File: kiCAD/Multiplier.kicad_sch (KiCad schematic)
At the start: 55 parts, among them IC2 ADG1221BRMZ, J1 Conn_01x02_Pin, J2 Conn_01x02_Pin, J3 Conn_01x01_Pin, Q1 BC846BPN, Q2 BC846BPN, U1 TS912, U10 TPS63060, U2 LM339, U4 TS912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

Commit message: Replacing schematics for TLV3402IDR assigning footpritns and adding first PCB layout
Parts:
- removed J3: Conn_01x01_Pin, Connector_PinHeader_2.54mm:PinHeader_1x01_P2.54mm_Vertical, symbol Connector:Conn_01x01_Pin
- removed Q1, Q2: BC846BPN, Package_TO_SOT_SMD:SOT-363_SC-70-6, symbol Transistor_BJT:BC846BPN
- removed U2: LM339, Custom:LM339_SOIC14, symbol Comparator:LM339
- added J3: Conn_01x02_Pin, Connector_PinHeader_2.54mm:PinHeader_1x02_P2.54mm_Vertical, symbol Connector:Conn_01x02_Pin
- added Q7, Q8: Q_Dual_PNP_PNP_C1B1B2C2E2E1, Custom:SOT-363_DUAL_PNP, symbol Device:Q_Dual_PNP_PNP_C1B1B2C2E2E1
- added R27, R28: 10k, Resistor_SMD:R_0805_2012Metric_Pad1.20x1.40mm_HandSolder, symbol Device:R
- added U2, U7: TLV340, Custom:TLV3402IDR_SOIC8, symbol Amplifier_Operational:TS912
- C1: footprint Capacitor_SMD:C_0805_2012Metric -> Resistor_SMD:R_0805_2012Metric_Pad1.20x1.40mm_HandSolder
- R6: value 2k -> 10k
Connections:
- net GND: now also J3.1 (Pin_1), U2.4 (V-), U7.4 (V-)
- net Ux+Er: now also U2.3 (+)
- net UxUy: now also J3.2 (Pin_2)
- net VCC: now also Q7.5 (E2), Q8.6 (E1), U2.8 (V+), U7.8 (V+)
- net at R1.2, RV2.1: now also U2.7, U7.3 (+)
- net at R11.1, U1.7: now also R28.2; no longer U1.6 (-)
- net at C1.1: now also Q8.4 (C2), U2.2 (-), U2.6 (-), U7.1
- net at R3.1, R4.2, RV2.2: now also U2.5 (+), U7.2 (-)
- net at R5.1: now also Q7.1 (C1), Q7.2 (B1), Q8.3 (B2)
- net at R10.1, U1.1: now also R27.2; no longer U1.2 (-)
- net IN1 renamed PWM_OUT
- net PWM_OUT: now also U2.1
- new net: Q7.3 (B2), Q7.6 (E1), Q8.1 (C1), Q8.2 (B1)
- new net: Q7.4 (C2), Q8.5 (E2)
- new net: R27.1, U1.2 (-)
- new net: R28.1, U1.6 (-)
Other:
- note added: "Buck-boost converter"
- note added: "Er dobieramy tak by było równe kV wzmacniacza U6A Er dodajemy do syg wejściowego Ux"
- note added: "INPUT SIGNALS"
- note added: "OUTPUT SIGNAL"
- note added: "Power Supply"
- note added: "Uy buffer"
- note added: "kV = Er"
- note added: "kV=Er by skompensować dodawanie Er do sygnału Ux"
- note removed: "DLa Er=1.8V R23"
- note removed: "Er dobieramy tak by było równe Amp_saw Er dodajemy do syg wejściowego Ux"
- note removed: "LDO"
- note removed: "TLV340"
- note removed: "Ten zamienić"
- note removed: "Tutaj znależć scalaka step down/up"
- moved on the sheet: C1, C10, C11, C12, C2, C3, C4, C5, C6, C7, C8, C9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

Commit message: adding potentiometer
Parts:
- removed R21: 4k, Resistor_SMD:R_0805_2012Metric_Pad1.20x1.40mm_HandSolder, symbol Device:R
- added RV4: 1,1k, Potentiometer_SMD:Potentiometer_Bourns_3314G_Vertical, symbol Device:R_Potentiometer
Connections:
- net GND: now also RV4.3
- net at U5.2 (-): now also RV4.1; no longer R22.2
- new net: R22.2, RV4.2
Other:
- note added: "Cascode current mirror PNP"
- note added: "Sawtooth"
- moved on the sheet: C1, C2, C3, IC2, R1, R15, R16, R17, R18, R2, R20, R22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

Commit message: Modified:  Multiplier.kicad_sch (resistors values)
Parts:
- R22: value 3k -> 7,5k
- R3: value 25k -> 24k
- RV1: value 1,1k -> 1,15k
- RV2: value 12k -> 12,5k
- RV3: value 1,1k -> 2,4k
- RV4: value 1,1k -> 3k
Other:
- note added: "Amp_saw = Vcc*R3/(R4||Rv2+R3) ~= 3.5V"
- note added: "Asaw dobieramy tak, aby było większe niż Er + 1.5"
- note added: "Buffered inputs"
- note added: "Er = RV1/(R19+RV1) * Vcc = 1.825V"
- note added: "Er dobieramy tak by było równe kV wzmacniacza U6A i większe od minimalnej wartości Ux (-1.5 V) Er dodajemy do syg wejściowego Ux"
- note added: "Four-Quadrant Multiplier Input voltages (Ux, Uy) range: < -1.5V, 1.5V > Voltage supply range: 4.5-6 V"
- note added: "Iout/Iref ~= 0.99"
- note added: "Non inverting op amp with k = Asaw"
- note added: "Non inverting op amp with k = Er"
- note added: "k = 1 + R22/RV4 = 3.5 = Asaw"
- note added: "k = 1 + R23/RV3 = 1.833 ~= Er"
- note removed: "* dla obecnych wartości Amp_saw = 3.5V"
- note removed: "Amp_saw = Vcc*R3/(R4||Rv2+R3)"
- note removed: "Er = 1,808V dla r19=15k, rv1=8,5k"
- note removed: "Er dobieramy tak by było równe kV wzmacniacza U6A Er dodajemy do syg wejściowego Ux"
- note removed: "Iout/Iref ~= 0,99"
- note removed: "dla R3=4.7k, RV2=9.5k, R4=100k Amp_saw = 1.757V"
- note removed: "kV = Er"
- note removed: "kV=Er by skompensować dodawanie Er do sygnału Ux"
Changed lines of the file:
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@@
     (fill (type none))
+  )
+  (text "Non inverting op amp with k = Er\n\n" (at 205.74 134.62 0)
+    (effects (font (size 0.9 0.9)) (justify left bottom))
   )
   (text "Cascode current mirror PNP" (at 35.56 21.59 0)
@@
     (effects (font (size 1.27 1.27)) (justify left bottom))
   )
-  (text "Er = 1,808V dla r19=15k, rv1=8,5k" (at 49.53 191.77 0)
-    (effects (font (size 0.7 0.7)) (justify left bottom))
-  )
-  (text "RMS\n\n" (at 231.14 105.41 0)
+  (text "Non inverting op amp with k = Asaw\n\n" (at 175.26 99.06 0)
+    (effects (font (size 0.9 0.9)) (justify left bottom))
+  )
+  (text "Buffered inputs" (at 12.7 125.73 0)
+    (effects (font (size 1.27 1.27)) (justify left bottom))
+  )
+  (text "RMS\n\n" (at 138.43 100.33 0)
     (effects (font (size 1.27 1.27)) (justify left bottom))
   )
@@
     (effects (font (size 1.27 1.27)) (justify left bottom))
   )
-  (text "Er dobieramy tak by było równe kV wzmacniacza U6A\nEr dodajemy do syg wejściowego Ux\n"
-    (at 49.53 190.5 0)
-    (effects (font (size 0.7 0.7)) (justify left bottom))
-  )
-  (text "kV=Er by skompensować dodawanie Er do sygnału Ux\n" (at 210.82 134.62 0)
+  (text "Four-Quadrant Multiplier\nInput voltages (Ux, Uy) range:\n < -1.5V, 1.5V > \nVoltage supply range: 4.5-6 V"
+    (at 88.9 24.13 0)
+    (effects (font (size 1.5 1.5) (thickness 0.3) bold) (justify left bottom))
+  )
+  (text "Er dobieramy tak by było równe kV wzmacniacza U6A\ni większe od minimalnej wartości Ux (-1.5 V)\nEr dodajemy do syg wejściowego Ux\n"
+    (at 49.53 191.77 0)
     (effects (font (size 0.7 0.7)) (justify left bottom))
   )
@@
     (effects (font (size 1.27 1.27)) (justify left bottom))
   )
-  (text "Power Supply\n\n" (at 267.97 81.28 0)
-    (effects (font (size 127 127)) (justify left bottom))
+  (text "Asaw dobieramy tak, aby było większe niż Er + 1.5" (at 40.64 67.31 0)
+    (effects (font (size 0.9 0.9)) (justify left bottom))
   )
   (text "INPUT SIGNALS\n" (at 17.78 167.64 0)
     (effects (font (size 1.27 1.27)) (justify left bottom))
   )
+  (text "Er = RV1/(R19+RV1) * Vcc = 1.825V" (at 49.53 187.96 0)
+    (effects (font (size 0.7 0.7)) (justify left bottom))
+  )
   (text "Sawtooth\n" (at 85.09 73.66 0)
     (effects (font (size 1.27 1.27)) (justify left bottom))
   )
-  (text "dla R3=4.7k, RV2=9.5k, R4=100k Amp_saw = 1.757V" (at 40.64 69.85 0)
-    (effects (font (size 0.9 0.9)) (justify left bottom))
-  )
   (text "Subtractor\n" (at 240.03 105.41 0)
     (effects (font (size 1.27 1.27)) (justify left bottom))
   )
-  (text "Amp_saw = Vcc*R3/(R4||Rv2+R3)" (at 40.64 67.31 0)
+  (text "k = 1 + R22/RV4 = 3.5 = Asaw\n" (at 195.58 120.65 0)
     (effects (font (size 0.9 0.9)) (justify left bottom))
   )
-  (text "kV = Er" (at 219.71 133.35 0)
-    (effects (font (size 1.27 1.27)) (justify left bottom))
-  )
-  (text "Iout/Iref ~= 0,99\n" (at 57.15 52.07 0)
+  (text "Iout/Iref ~= 0.99\n" (at 57.15 52.07 0)
     (effects (font (size 0.7 0.7)) (justify left bottom))
   )
@@
     (effects (font (size 1.27 1.27)) (justify left bottom))
   )
+  (text "k = 1 + R23/RV3 = 1.833 ~= Er\n\n" (at 219.71 157.48 0)
+    (effects (font (size 0.9 0.9)) (justify left bottom))
+  )
   (text "Buck-boost converter\n" (at 219.71 20.32 0)
     (effects (font (size 1.27 1.27)) (justify left bottom))
@@
     (effects (font (size 1.27 1.27)) (justify right bottom))
   )
-  (text "* dla obecnych wartości Amp_saw = 3.5V" (at 40.64 68.58 0)
+  (text "Amp_saw = Vcc*R3/(R4||Rv2+R3) ~= 3.5V" (at 40.64 64.77 0)
     (effects (font (size 0.9 0.9)) (justify left bottom))
   )
@@
       (effects (font (size 1.27 1.27)) (justify right))
     )
-    (property "Value" "1,1k" (at 185.42 115.57 0)
+    (property "Value" "3k" (at 185.42 115.57 0)
       (effects (font (size 1.27 1.27)) (justify right))
     )
@@
       (effects (font (size 1.27 1.27)) (justify right))
     )
-    (property "Value" "1,1k" (at 68.58 185.42 90)
+    (property "Value" "1,15k" (at 68.58 185.42 90)
       (effects (font (size 1.27 1.27)) (justify right))
     )
@@
       (effects (font (size 1.27 1.27)))
     )
-    (property "Value" "3k" (at 200.66 111.76 90)
+    (property "Value" "7,5k" (at 200.66 111.76 90)
       (effects (font (size 1.27 1.27)))
     )
@@
       (effects (font (size 1.27 1.27)) (justify right))
     )
-    (property "Value" "12k" (at 39.37 86.36 0)
+    (property "Value" "12,5k" (at 39.37 86.36 0)
       (effects (font (size 1.27 1.27)) (justify right))
     )
@@
       (effects (font (size 1.27 1.27)) (justify left))
     )
-    (property "Value" "25k" (at 41.91 99.06 0)
+    (property "Value" "24k" (at 41.91 99.06 0)
       (effects (font (size 1.27 1.27)) (justify left))
     )
@@
       (effects (font (size 1.27 1.27)) (justify right))
     )
-    (property "Value" "1,1k" (at 212.09 151.13 0)
+    (property "Value" "2,4k" (at 212.09 151.13 0)
       (effects (font (size 1.27 1.27)) (justify right))
     )

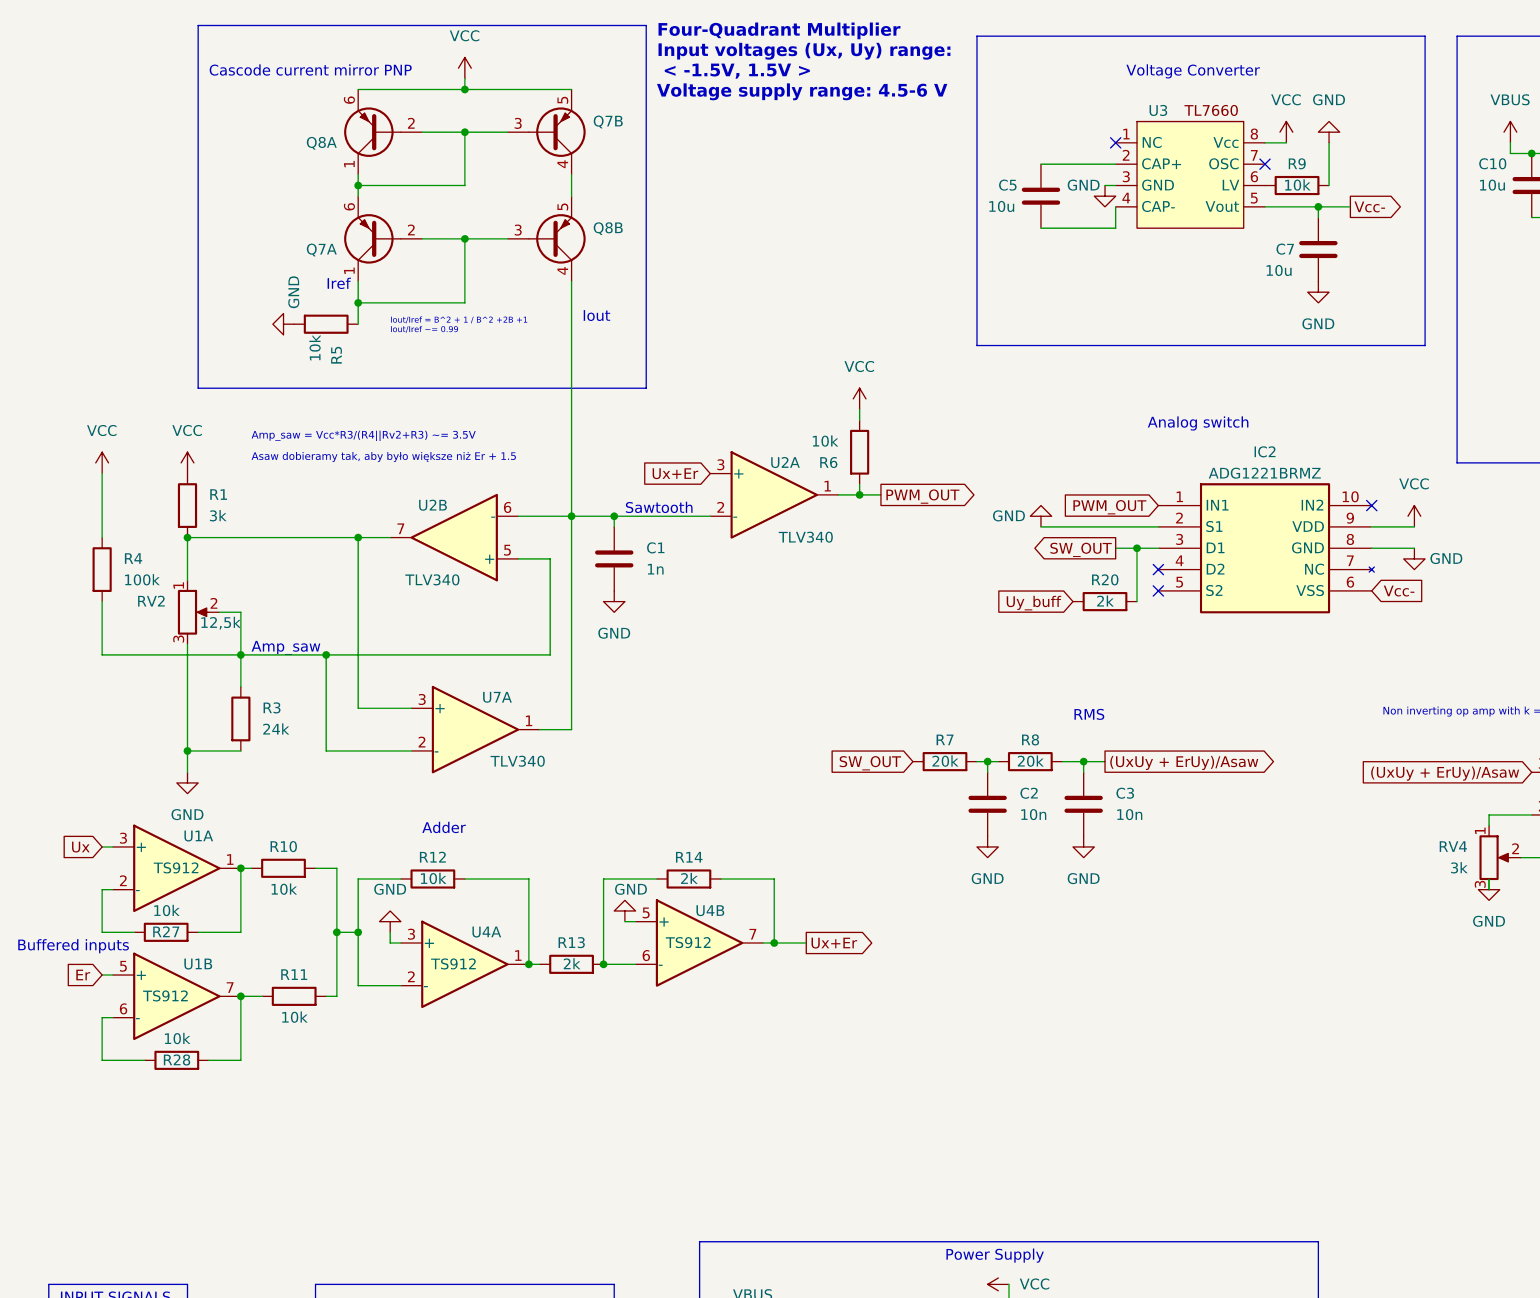
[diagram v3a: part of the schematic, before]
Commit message: New footprint for buck-boost converter
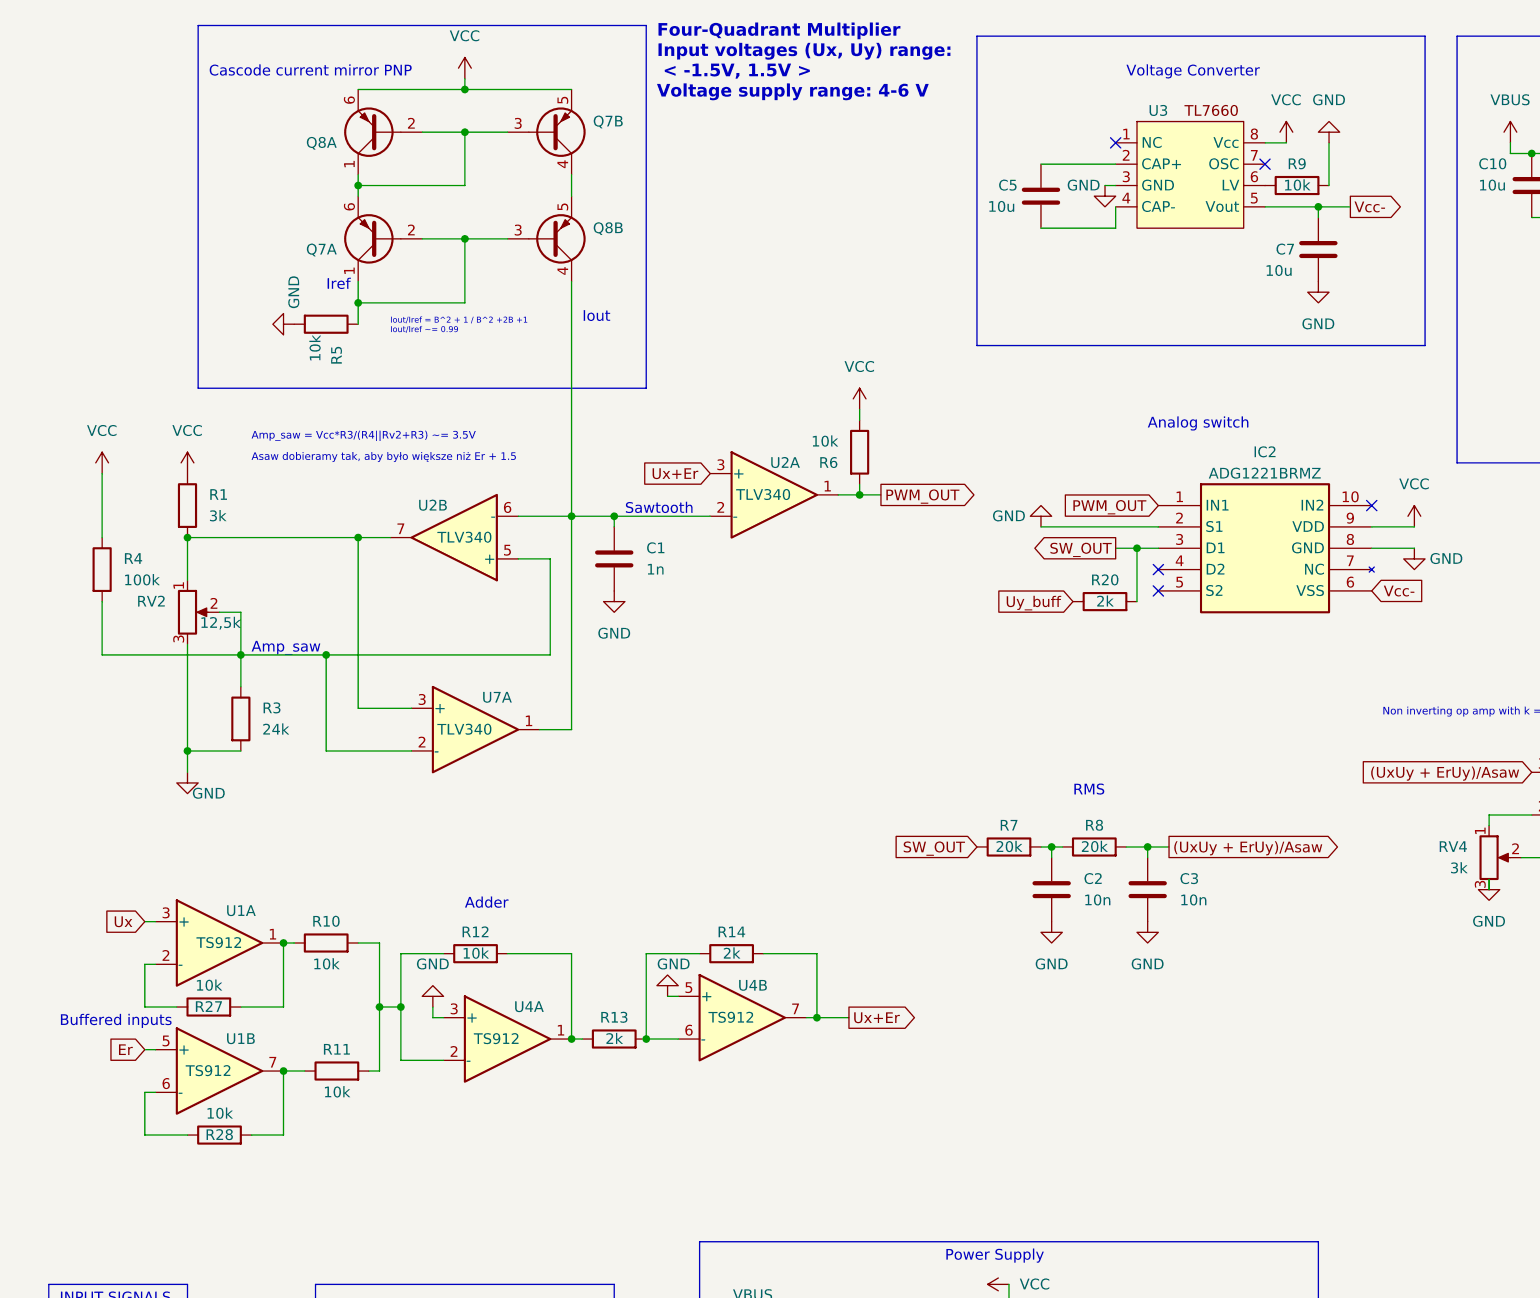
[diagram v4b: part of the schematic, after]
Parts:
- U10: footprint Package_SON:Texas_S-PWSON-N10_ThermalVias -> Custom:Texas_S-PWSON-N10_ThermalVias_Custom
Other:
- note added: "Four-Quadrant Multiplier Input voltages (Ux, Uy) range: < -1.5V, 1.5V > Voltage supply range: 4-6 V"
- note removed: "Four-Quadrant Multiplier Input voltages (Ux, Uy) range: < -1.5V, 1.5V > Voltage supply range: 4.5-6 V"
- moved on the sheet: C2, C3, R10, R11, R12, R13, R14, R27, R28, R7, R8, U1A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
